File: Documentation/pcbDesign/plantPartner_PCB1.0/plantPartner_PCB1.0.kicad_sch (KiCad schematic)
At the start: 75 parts, among them IC1 MPM3610, J1 Conn_01x04, J10 Screw_Terminal_01x03, J11 Conn_01x04, J12 Conn_01x03, J13 Conn_01x03, J14 Conn_01x03, J15 Conn_01x03, J16 Conn_01x04, J17 Conn_01x03, J18 Screw_Terminal_01x02, J19 Barrel_Jack, J2 Conn_01x04, J20 Conn_02x04_Top_Bottom, J21 Conn_01x04, J22 Conn_01x04, J23 Conn_01x02, J25 Conn_01x04, J26 Conn_01x01, J27 Conn_01x03, J3 Conn_01x04, J4 Screw_Terminal, J5 Conn_01x02, J6 Screw_Terminal_01x03, J7 Conn_01x03, J8 Conn_02x04_Top_Bottom, J9 Conn_01x03, K1 SRD-05VDC-SL-C, K2 SRD-05VDC-SL-C, Q1 PNP, Q2 PNP, U1 EL357N-G, U2 MAX485, U3 ESP32-DEVKIT-V1, U4 EL357N-G

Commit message: Finished RS485 Transceiver, working on Buck Converter and connecting signals
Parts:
- removed J11: Conn_01x04, Connector_PinHeader_2.54mm:PinHeader_1x04_P2.54mm_Vertical, symbol Connector_Generic:Conn_01x04
- added J11: Conn_01x02, Connector_PinHeader_2.54mm:PinHeader_1x02_P2.54mm_Vertical, symbol Connector_Generic:Conn_01x02
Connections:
- net +12V: now also J11.2 (Pin_2); no longer J26.1 (Pin_1), J27.1 (Pin_1), U1.2, U3.27 (D12), U3.28 (D13), U4.2
- net ADC1_4/Touch9: now also J20.3 (Pin_3); no longer J20.8 (Pin_8)
- net ADC1_5/Touch8: now also J20.4 (Pin_4); no longer J20.3 (Pin_3)
- net ADC2_0/Touch0: now also J20.8 (Pin_8); no longer J20.4 (Pin_4)
- net GND: now also J11.1 (Pin_1)
- new net PWM_FERTIL_PIN: J27.1 (Pin_1), U1.2, U3.28 (D13)
- new net PWM_WATER_PIN: J26.1 (Pin_1), U3.27 (D12), U4.2

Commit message: Fixed Buck Converter and routed it. Connected more majority of ESP signals and some of the debugging pins. Brought the size of PCB down to about 1/2 of the original. My goal is to finish by today and optimize size in the 2nd gen
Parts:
- removed J23: Conn_01x02, Connector_PinHeader_2.54mm:PinHeader_1x02_P2.54mm_Vertical, symbol Connector_Generic:Conn_01x02
- removed J25: Conn_01x04, Connector_PinHeader_2.54mm:PinHeader_1x04_P2.54mm_Vertical, symbol Connector_Generic:Conn_01x04
- removed J27: Conn_01x03, Connector_PinHeader_2.54mm:PinHeader_1x03_P2.54mm_Vertical, symbol Connector_Generic:Conn_01x03
- added J23, J27, J28: Conn_01x01, Connector_PinHeader_2.54mm:PinHeader_1x01_P2.54mm_Vertical, symbol Connector_Generic:Conn_01x01
- added J24, J25: Conn_01x03, Connector_PinHeader_2.54mm:PinHeader_1x03_P2.54mm_Vertical, symbol Connector_Generic:Conn_01x03
- IC1: footprint buckConverter:MPM3610 -> MPM3610:MPM3610
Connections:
- net ADC2_0/Touch0: now also J24.3 (Pin_3); no longer J20.8 (Pin_8)
- net ADC2_3/Touch3: now also J24.1 (Pin_1)
- net ADC_LIGHT_SENSOR: now also J25.2 (Pin_2)
- net ADC_MOISTURE_SENSOR: now also J25.3 (Pin_3)
- net ESP_3.3V: now also J28.1 (Pin_1)
- net ESP_EN: now also J25.1 (Pin_1)
- net EXTERNAL LED: now also J23.1 (Pin_1)
- net GND: now also J20.8 (Pin_8), J8.3 (Pin_3); no longer J8.4 (Pin_4)
- net INTERNAL LED: now also J24.2 (Pin_2)
- net MISO/VSPI_MISO: now also J8.4 (Pin_4); no longer J8.3 (Pin_3)
- net PWM_FERTIL_PIN: now also J27.1 (Pin_1)
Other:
- moved on the sheet: D10, R22

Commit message: Finished Routing (for now). I need to add silkscreens for debugging, then copper pour and probably other stuff. My goal is so have a JLCPCB order by tomorrow. I brought the PCB down to about the size of my phone
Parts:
- added J29: Conn_01x02, Connector_PinHeader_2.54mm:PinHeader_1x02_P2.54mm_Vertical, symbol Connector_Generic:Conn_01x02
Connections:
- net +12V: no longer C3.1, C4.1, J3.1 (Pin_1), R10.1, R4.1, R5.1, R6.1, R7.1, R8.1, U2.8 (VCC)
- net +5V: now also C3.1, C4.1, J3.1 (Pin_1), R10.1, R4.1, R5.1, R6.1, R7.1, R8.1, U2.8 (VCC)
- net ADC_LIGHT_SENSOR: now also J29.2 (Pin_2)
- net ADC_MOISTURE_SENSOR: now also J29.1 (Pin_1)
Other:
- moved on the sheet: J25

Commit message: Finished Labeling PCB (too much) and fixed DRC errors on PCB. Time to add copper pours, drill holes, and probably more, then review it with a TA, and make the order :)
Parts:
- C3: footprint Capacitor_SMD:C_0201_0603Metric -> Capacitor_SMD:C_0603_1608Metric
- R8: footprint Resistor_SMD:R_0201_0603Metric -> Resistor_SMD:R_0603_1608Metric
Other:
- note added: "Route PCB Find best SMDs for Resistors, LEDs, and Capacitors"
- note removed: "Route PCB"
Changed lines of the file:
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@@
 		(comment 1 "PCB Lead Design: Carter Kreis")
 	)
-	(text "Route PCB\n"
-		(exclude_from_sim no)
-		(at 337.82 92.964 0)
-		(effects
-			(font
-				(size 1.27 1.27)
-			)
-		)
-	)
 	(text "Buck Converter (12V In to 5V Out 1.2A)"
 		(exclude_from_sim no)
@@
 		)
 	)
-	(text "Route PCB"
-		(exclude_from_sim no)
-		(at 338.328 95.504 0)
-		(effects
-			(font
-				(size 0.889 0.889)
-			)
-		)
-	)
 	(text "5V Relay - Water Pump\n\n\n"
 		(exclude_from_sim no)
@@
 		)
 	)
-	(text "Route PCB\n"
-		(exclude_from_sim no)
-		(at 337.312 89.916 0)
-		(effects
-			(font
-				(size 1.524 1.524)
-			)
-		)
-	)
-	(text "Route PCB"
+	(text "Route PCB\nFind best SMDs for Resistors, LEDs, and Capacitors"
 		(exclude_from_sim no)
 		(at 337.566 85.598 0)
@@
 			)
 		)
-		(property "Footprint" "Capacitor_SMD:C_0201_0603Metric"
+		(property "Footprint" "Capacitor_SMD:C_0603_1608Metric"
 			(at 53.0352 132.08 0)
 			(effects
@@
 			)
 		)
-		(property "Footprint" "Resistor_SMD:R_0201_0603Metric"
+		(property "Footprint" "Resistor_SMD:R_0603_1608Metric"
 			(at 69.342 125.73 90)
 			(effects

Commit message: Meeting with Tyler. I tried to implement Lamp Circuit with MOSFET but having trouble simulating it in LTspice
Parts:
- added J30: Screw_Terminal_01x02, symbol Connector:Screw_Terminal_01x02
- added Q4: AO3400A, Package_TO_SOT_SMD:SOT-23, symbol Transistor_FET:AO3400A
- added R25: 100, symbol Device:R
- added R27: 10k, symbol Device:R
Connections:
- net +5V: now also J30.2 (Pin_2)
- net GND: now also Q4.2 (S), R27.2
- new net: Q4.1 (G), R25.2, R27.1
- new net: J30.1 (Pin_1), Q4.3 (D)
- new net LAMP_PIN: R25.1

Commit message: Added Lamp to PCB. Added Copper Pours and Drill Holes. Now fixing rude error about cap. not getting copper pour connection properly
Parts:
- C3: footprint Capacitor_SMD:C_0603_1608Metric -> Capacitor_SMD:C_0201_0603Metric
- J30: footprint (none) -> TerminalBlock_Phoenix:TerminalBlock_Phoenix_MKDS-1,5-2-5.08_1x02_P5.08mm_Horizontal
- R25, R27: footprint (none) -> Resistor_SMD:R_0201_0603Metric
- R8: footprint Resistor_SMD:R_0603_1608Metric -> Resistor_SMD:R_0201_0603Metric
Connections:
- net ADC1_6 is gone; now on net LAMP_PIN: J20.1 (Pin_1), U3.19 (D34)
- net Gate: now reaches Q4.1 (G), R25.2, R27.1
- net Drain: now reaches J30.1 (Pin_1), Q4.3 (D)
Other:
- moved on the sheet: J30, Q4, R25, R27

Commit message: Gerber and Drill files have been generated. I will order on JLCPCB tomorrow morning ASAP and then finish up cube for Beta
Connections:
- net +12V: no longer IC1.2 (VCC)
- net GND: no longer IC1.11 (BST), IC1.18 (AAM), IC1.4 (SW), IC1.5 (SW), IC1.6 (SW)
- new net SW: IC1.4 (SW), IC1.5 (SW), IC1.6 (SW)
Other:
- note added: "MOSFET Lamp Circuit"
- note removed: "Route PCB Find best SMDs for Resistors, LEDs, and Capacitors"
- note removed: "Run Electrical Rules Checker and make sure Schematic Passes."

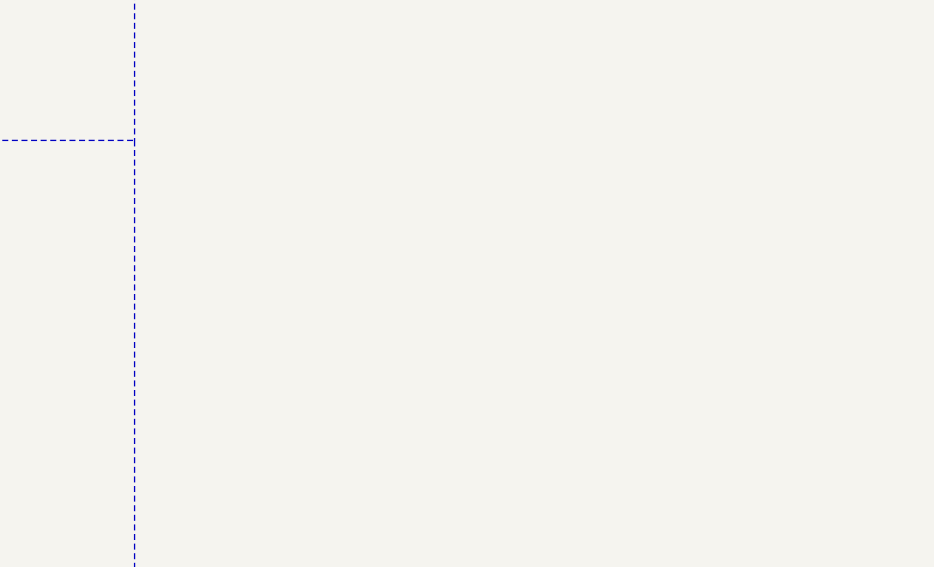
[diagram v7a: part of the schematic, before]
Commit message: I got the plugin finally working! I had some messed up Python modules that I had to remove and then reinstall. I have also now learned that the footprints I chose for the PCB were too small and classified as extended for JLCPCB which means more 4189. So now I have to change all the Resistor, Capacitor, and Diode footprints to a bigger size to not cost too much. This will then also result in me having to route these small parts again. I am tired of my lack of PCB design knowledge but I think I might be done after this.
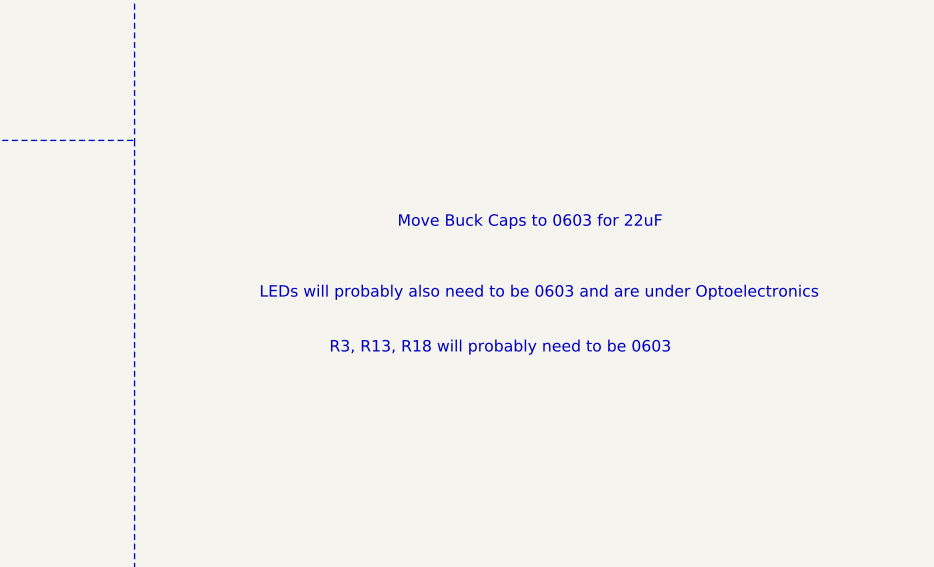
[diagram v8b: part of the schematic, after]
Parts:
- C1, C2, C3, C4: footprint Capacitor_SMD:C_0201_0603Metric -> Capacitor_SMD:C_0402_1005Metric
- D1, D10, D11, D2, D3, D5, D6: footprint LED_SMD:LED_0201_0603Metric -> LED_SMD:LED_0402_1005Metric
- R1, R10, R11, R12, R13, R14, R15, R16, R17, R18, R19, R2, R20, R21, R22, R23, R24, R25, R26, R27, R3, R4, R5, R6, R7, R8, R9: footprint Resistor_SMD:R_0201_0603Metric -> Resistor_SMD:R_0402_1005Metric
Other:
- note added: "LEDs will probably also need to be 0603 and are under Optoelectronics"
- note added: "Move Buck Caps to 0603 for 22uF"
- note added: "R3, R13, R18 will probably need to be 0603"
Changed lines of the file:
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@@
 		)
 	)
+	(text "Move Buck Caps to 0603 for 22uF\n"
+		(exclude_from_sim no)
+		(at 320.802 96.774 0)
+		(effects
+			(font
+				(size 1.27 1.27)
+			)
+		)
+	)
 	(text "ESP-32 WROOM DEVKIT V1\n\n"
 		(exclude_from_sim no)
@@
 		)
 	)
+	(text "R3, R13, R18 will probably need to be 0603"
+		(exclude_from_sim no)
+		(at 317.5 110.744 0)
+		(effects
+			(font
+				(size 1.27 1.27)
+			)
+		)
+	)
+	(text "LEDs will probably also need to be 0603 and are under Optoelectronics"
+		(exclude_from_sim no)
+		(at 321.818 104.648 0)
+		(effects
+			(font
+				(size 1.27 1.27)
+			)
+		)
+	)
 	(text "5V Relay - Fertilizer Pump\n"
 		(exclude_from_sim no)
@@
 			)
 		)
-		(property "Footprint" "Resistor_SMD:R_0201_0603Metric"
+		(property "Footprint" "Resistor_SMD:R_0402_1005Metric"
 			(at 186.182 58.42 90)
 			(effects
@@
 			)
 		)
-		(property "Footprint" "Resistor_SMD:R_0201_0603Metric"
+		(property "Footprint" "Resistor_SMD:R_0402_1005Metric"
 			(at 298.45 30.988 90)
 			(effects
@@
 			)
 		)
-		(property "Footprint" "Resistor_SMD:R_0201_0603Metric"
+		(property "Footprint" "Resistor_SMD:R_0402_1005Metric"
 			(at 84.582 45.72 90)
 			(effects
@@
 			)
 		)
-		(property "Footprint" "Resistor_SMD:R_0201_0603Metric"
+		(property "Footprint" "Resistor_SMD:R_0402_1005Metric"
 			(at 186.182 133.35 90)
 			(effects
@@
 			)
 		)
-		(property "Footprint" "Resistor_SMD:R_0201_0603Metric"
+		(property "Footprint" "Resistor_SMD:R_0402_1005Metric"
 			(at 99.822 261.62 90)
 			(effects
@@
 			)
 		)
-		(property "Footprint" "Resistor_SMD:R_0201_0603Metric"
+		(property "Footprint" "Resistor_SMD:R_0402_1005Metric"
 			(at 139.192 35.56 90)
 			(effects
@@
 			)
 		)
-		(property "Footprint" "LED_SMD:LED_0201_0603Metric"
+		(property "Footprint" "LED_SMD:LED_0402_1005Metric"
 			(at 71.12 135.89 0)
 			(effects
@@
 			)
 		)
-		(property "Footprint" "LED_SMD:LED_0201_0603Metric"
+		(property "Footprint" "LED_SMD:LED_0402_1005Metric"
 			(at 187.96 142.24 0)
 			(effects
@@
 			)
 		)
-		(property "Footprint" "LED_SMD:LED_0201_0603Metric"
+		(property "Footprint" "LED_SMD:LED_0402_1005Metric"
 			(at 187.96 67.31 0)
 			(effects
@@
 			)
 		)
-		(property "Footprint" "Resistor_SMD:R_0201_0603Metric"
+		(property "Footprint" "Resistor_SMD:R_0402_1005Metric"
 			(at 87.122 82.55 90)
 			(effects
@@
 			)
 		)
-		(property "Footprint" "Resistor_SMD:R_0201_0603Metric"
+		(property "Footprint" "Resistor_SMD:R_0402_1005Metric"
 			(at 88.9 232.918 90)
 			(effects
@@
 			)
 		)
-		(property "Footprint" "Resistor_SMD:R_0201_0603Metric"
+		(property "Footprint" "Resistor_SMD:R_0402_1005Metric"
 			(at 31.242 93.98 90)
 			(effects
@@
 			)
 		)
-		(property "Footprint" "Resistor_SMD:R_0201_0603Metric"
+		(property "Footprint" "Resistor_SMD:R_0402_1005Metric"
 			(at 43.942 93.98 90)
 			(effects
@@
 			)
 		)
-		(property "Footprint" "Resistor_SMD:R_0201_0603Metric"
+		(property "Footprint" "Resistor_SMD:R_0402_1005Metric"
 			(at 182.88 46.228 90)
 			(effects
@@
 			)
 		)
-		(property "Footprint" "Resistor_SMD:R_0201_0603Metric"
+		(property "Footprint" "Resistor_SMD:R_0402_1005Metric"
 			(at 182.88 121.158 90)
 			(effects
@@
 			)
 		)
-		(property "Footprint" "Resistor_SMD:R_0201_0603Metric"
+		(property "Footprint" "Resistor_SMD:R_0402_1005Metric"
 			(at 82.55 184.658 90)
 			(effects
@@
 			)
 		)
-		(property "Footprint" "LED_SMD:LED_0201_0603Metric"
+		(property "Footprint" "LED_SMD:LED_0402_1005Metric"
 			(at 140.97 120.65 0)
 			(effects
@@
 			)
 		)
-		(property "Footprint" "Resistor_SMD:R_0201_0603Metric"
+		(property "Footprint" "Resistor_SMD:R_0402_1005Metric"
 			(at 154.432 110.49 90)
 			(effects
@@
 			)
 		)
-		(property "Footprint" "Resistor_SMD:R_0201_0603Metric"
+		(property "Footprint" "Resistor_SMD:R_0402_1005Metric"
 			(at 76.962 92.71 90)
 			(effects
@@
 			)
 		)
-		(property "Footprint" "Capacitor_SMD:C_0201_0603Metric"
+		(property "Footprint" "Capacitor_SMD:C_0402_1005Metric"
 			(at 53.0352 132.08 0)
 			(effects
@@
 			)
 		)
-		(property "Footprint" "Resistor_SMD:R_0201_0603Metric"
+		(property "Footprint" "Resistor_SMD:R_0402_1005Metric"
 			(at 176.022 110.49 90)
 			(effects
@@
 			)
 		)
-		(property "Footprint" "Resistor_SMD:R_0201_0603Metric"
+		(property "Footprint" "Resistor_SMD:R_0402_1005Metric"
 			(at 139.192 110.49 90)
 			(effects
@@
 			)
 		)
-		(property "Footprint" "LED_SMD:LED_0201_0603Metric"
+		(property "Footprint" "LED_SMD:LED_0402_1005Metric"
 			(at 101.6 252.73 0)
 			(effects
@@
 			)
 		)
-		(property "Footprint" "Resistor_SMD:R_0201_0603Metric"
+		(property "Footprint" "Resistor_SMD:R_0402_1005Metric"
 			(at 27.94 33.528 90)
 			(effects
@@
 			)
 		)
-		(property "Footprint" "Resistor_SMD:R_0201_0603Metric"
+		(property "Footprint" "Resistor_SMD:R_0402_1005Metric"
 			(at 303.022 34.29 90)
 			(effects
@@
 			)
 		)
-		(property "Footprint" "Resistor_SMD:R_0201_0603Metric"
+		(property "Footprint" "Resistor_SMD:R_0402_1005Metric"
 			(at 84.582 34.29 90)
 			(effects
@@
 			)
 		)
-		(property "Footprint" "Capacitor_SMD:C_0201_0603Metric"
+		(property "Footprint" "Capacitor_SMD:C_0402_1005Metric"
 			(at 96.52 25.7048 0)
 			(effects
@@
 			)
 		)
-		(property "Footprint" "Resistor_SMD:R_0201_0603Metric"
+		(property "Footprint" "Resistor_SMD:R_0402_1005Metric"
 			(at 69.342 125.73 90)
 			(effects
@@
 			)
 		)
-		(property "Footprint" "Capacitor_SMD:C_0201_0603Metric"
+		(property "Footprint" "Capacitor_SMD:C_0402_1005Metric"
 			(at 27.94 25.0952 0)
 			(effects
@@
 			)
 		)
-		(property "Footprint" "Resistor_SMD:R_0201_0603Metric"
+		(property "Footprint" "Resistor_SMD:R_0402_1005Metric"
 			(at 82.042 125.73 90)
 			(effects
@@
 			)
 		)
-		(property "Footprint" "LED_SMD:LED_0201_0603Metric"
+		(property "Footprint" "LED_SMD:LED_0402_1005Metric"
 			(at 260.35 176.53 0)
 			(effects
@@
 			)
 		)
-		(property "Footprint" "Resistor_SMD:R_0201_0603Metric"
+		(property "Footprint" "Resistor_SMD:R_0402_1005Metric"
 			(at 24.892 93.98 90)
 			(effects
@@
 			)
 		)
-		(property "Footprint" "Resistor_SMD:R_0201_0603Metric"
+		(property "Footprint" "Resistor_SMD:R_0402_1005Metric"
 			(at 154.432 35.56 90)
 			(effects
@@
 			)
 		)
-		(property "Footprint" "LED_SMD:LED_0201_0603Metric"
+		(property "Footprint" "LED_SMD:LED_0402_1005Metric"
 			(at 140.97 45.72 0)
 			(effects
@@
 			)
 		)
-		(property "Footprint" "Capacitor_SMD:C_0201_0603Metric"
+		(property "Footprint" "Capacitor_SMD:C_0402_1005Metric"
 			(at 63.1952 132.08 0)
 			(effects
@@
 			)
 		)
-		(property "Footprint" "Resistor_SMD:R_0201_0603Metric"
+		(property "Footprint" "Resistor_SMD:R_0402_1005Metric"
 			(at 176.022 35.56 90)
 			(effects
@@
 			)
 		)
-		(property "Footprint" "Resistor_SMD:R_0201_0603Metric"
+		(property "Footprint" "Resistor_SMD:R_0402_1005Metric"
 			(at 262.128 185.42 90)
 			(effects
@@
 			)
 		)
-		(property "Footprint" "Resistor_SMD:R_0201_0603Metric"
+		(property "Footprint" "Resistor_SMD:R_0402_1005Metric"
 			(at 37.592 93.98 90)
 			(effects
